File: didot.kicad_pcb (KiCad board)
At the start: 2 copper layers, 151.1 x 118.1 mm, 68 parts, among them J1 JST_BATTERY, U1 nice!nano

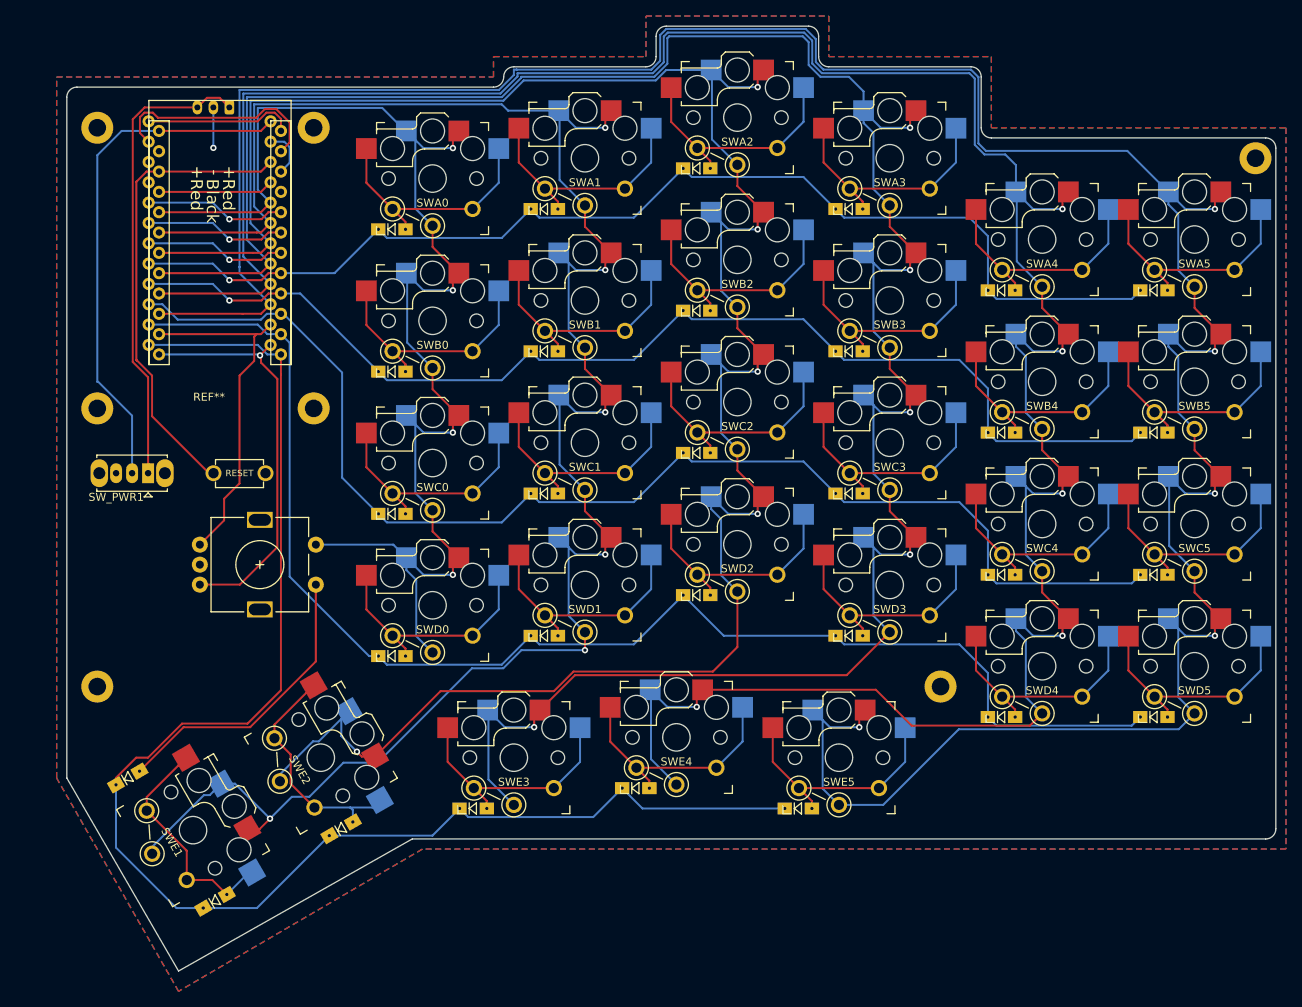
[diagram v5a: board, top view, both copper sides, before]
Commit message: Complete v1.0 layout with footprints
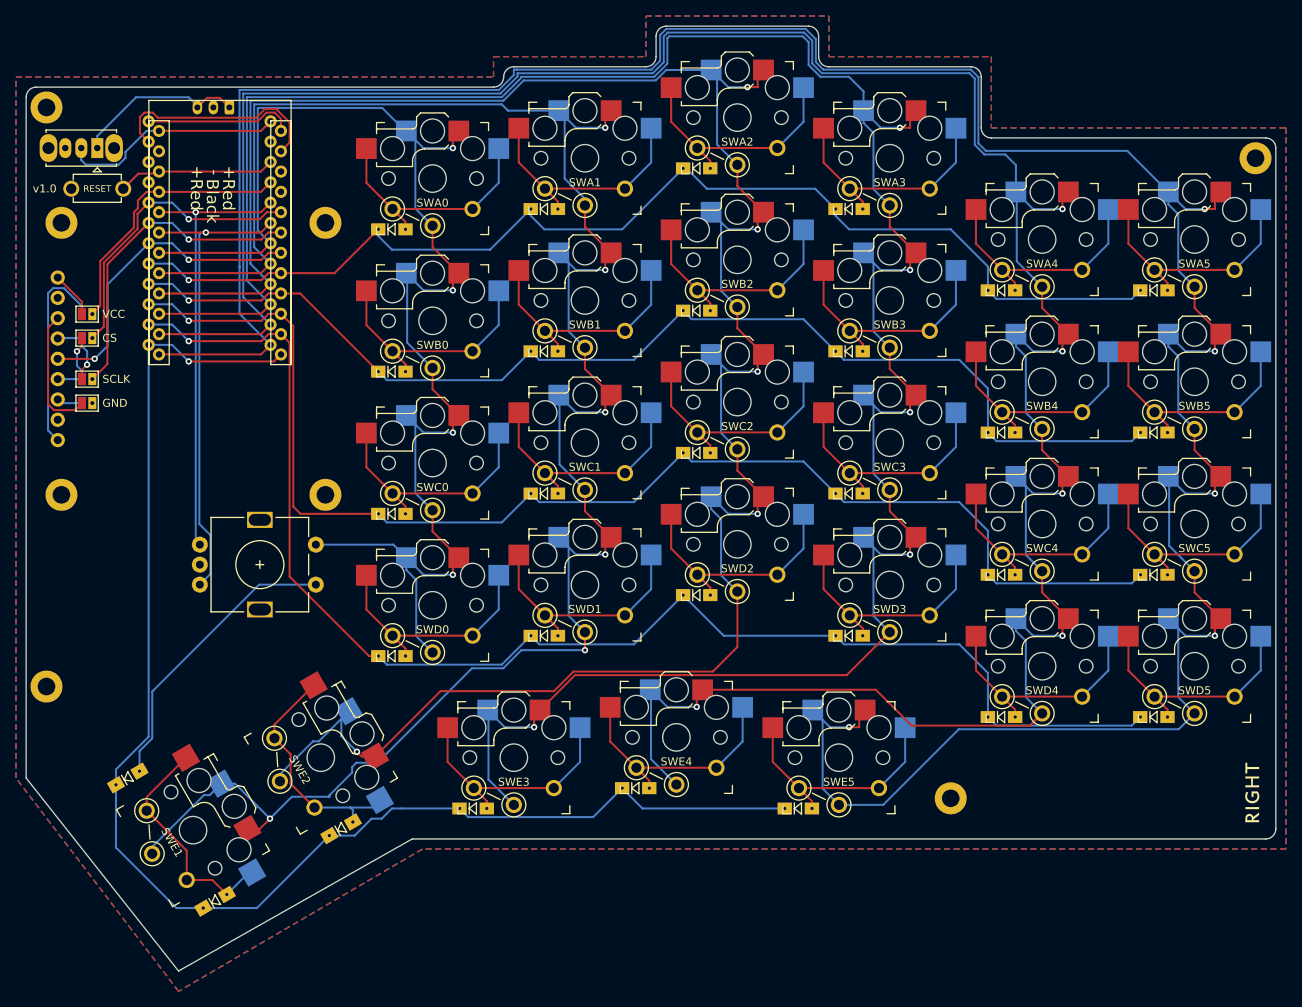
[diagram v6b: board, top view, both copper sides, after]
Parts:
- removed REF**: Waveshare_Sharp_LCD, Didot:Waveshare_Sharp_LCD
- removed the TH1 at (66.0, 102.9)
- added J2: Display Socket, Didot:1X09_ROUND_70, F.Cu at (61.1, 61.9)
- added JP1: VCC, Didot:ReversibleDisplayJumper, F.Cu at (64.8, 56.3)
- added JP2: CS, Didot:ReversibleDisplayJumper, F.Cu at (64.8, 59.3)
- added JP3: SCLK, Didot:ReversibleDisplayJumper, F.Cu at (64.8, 64.4)
- added JP4: GND, Didot:ReversibleDisplayJumper, F.Cu at (64.8, 67.4)
- added Ref**: Val**, Didot:didot_right, F.Cu at (194.3, 115.6)
- added TH1: HOLE, Didot:M2_HOLE_PCB, F.Cu at (61.6, 78.9)
- added TH1: HOLE, Didot:M2_HOLE_PCB, F.Cu at (94.6, 78.9)
- added TH1: HOLE, Didot:M2_HOLE_PCB, F.Cu at (94.6, 44.9)
- added TH1: HOLE, Didot:M2_HOLE_PCB, F.Cu at (61.6, 44.9)
- added TH1: HOLE, Didot:M2_HOLE_PCB, F.Cu at (59.7, 30.5)
- added TH1: HOLE, Didot:M2_HOLE_PCB, F.Cu at (59.7, 102.9)
- moved SW_PWR1 41.1 mm to (66.0, 35.6)
- moved SW_RESET1 39.8 mm to (66.0, 40.6), turned to 0 degrees
- moved TH1 14.0 mm to (172.7, 116.8)
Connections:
- U1 pad 13: ENCB -> col5
- U1 pad 14: ENCA -> col4
- U1 pad 15: col5 -> col3
- U1 pad 16: col4 -> col2
- U1 pad 17: col3 -> col1
- U1 pad 18: col2 -> col0
- U1 pad 19: col1 -> ENCB
- U1 pad 20: col0 -> ENCA
- U1 pad 21: Net-(U1-Pad21) -> VCOM
- U1 pad 5: Net-(U1-Pad5) -> CS
- U1 pad 6: Net-(U1-Pad6) -> SCLK
- U1 pad 7: Net-(U1-Pad7) -> MOSI
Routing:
- net SCLK: track 0.00 -> 40.2 mm, vias 0 -> 1
- net MOSI: track 0.00 -> 39.2 mm, vias 0 -> 2
- net RESET: track 58.6 -> 19.9 mm
- net CS: track 0.00 -> 37.6 mm, vias 0 -> 1
- net Net-(J1-Pad1): track 58.7 -> 21.7 mm
- net VCC: track 65.0 -> 28.1 mm
- net VCOM: track 0.00 -> 34.3 mm
- net Net-(J2-Pad9): track 0.00 -> 25.8 mm
- net Net-(U1-Pad6): track 17.8 -> 0.00 mm, vias 1 -> 0
- net Net-(U1-Pad5): track 17.8 -> 0.00 mm, vias 1 -> 0
- net Net-(U1-Pad7): track 17.8 -> 0.00 mm, vias 1 -> 0
- net Net-(J2-Pad3): track 0.00 -> 16.1 mm
- net Net-(U1-Pad21): track 14.4 -> 0.00 mm
- net GND: track 13.8 -> 0.05 mm, vias 1 -> 0
- net ENCA: track 43.9 -> 56.5 mm, vias 0 -> 1
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- added copper zone on B.Cu, net GND
- removed copper zone on B.Cu, net (none)
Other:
- board size 151.1 x 118.1 mm -> 156.2 x 118.1 mm
- board text added: "v1.0"
